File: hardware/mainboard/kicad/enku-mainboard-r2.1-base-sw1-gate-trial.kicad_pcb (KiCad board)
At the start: 4 copper layers, 59 x 101 mm, 132 parts, among them J1 1S LiPo + NTC, J2 Hirose DM3AT-SF-PEJM5, J3 FH34SRJ-24S-0.5SH(50), J5 GCT USB4105-GF-A-120, J6 4-pin pogo dock, J7 Tag-Connect TC2030-IDC-NL, Q1 IRLML6346TRPBF, Q2 AO3401A, SW1 HARD POWER, SW2 BOOT / RECOVERY, SW3 BTN_L1, SW4 BTN_L2, SW5 BTN_R1, SW6 BTN_R2, U1 ESP32-S3-WROOM-1-N16R8, U10 TLV3012BIDBVR, U2 TPS2121, U3 BQ25185DLHR, U4 TPS63802DLAR, U5 BMI270, U8 USBLC6-2SC6, U9 TMUX1101DBVR

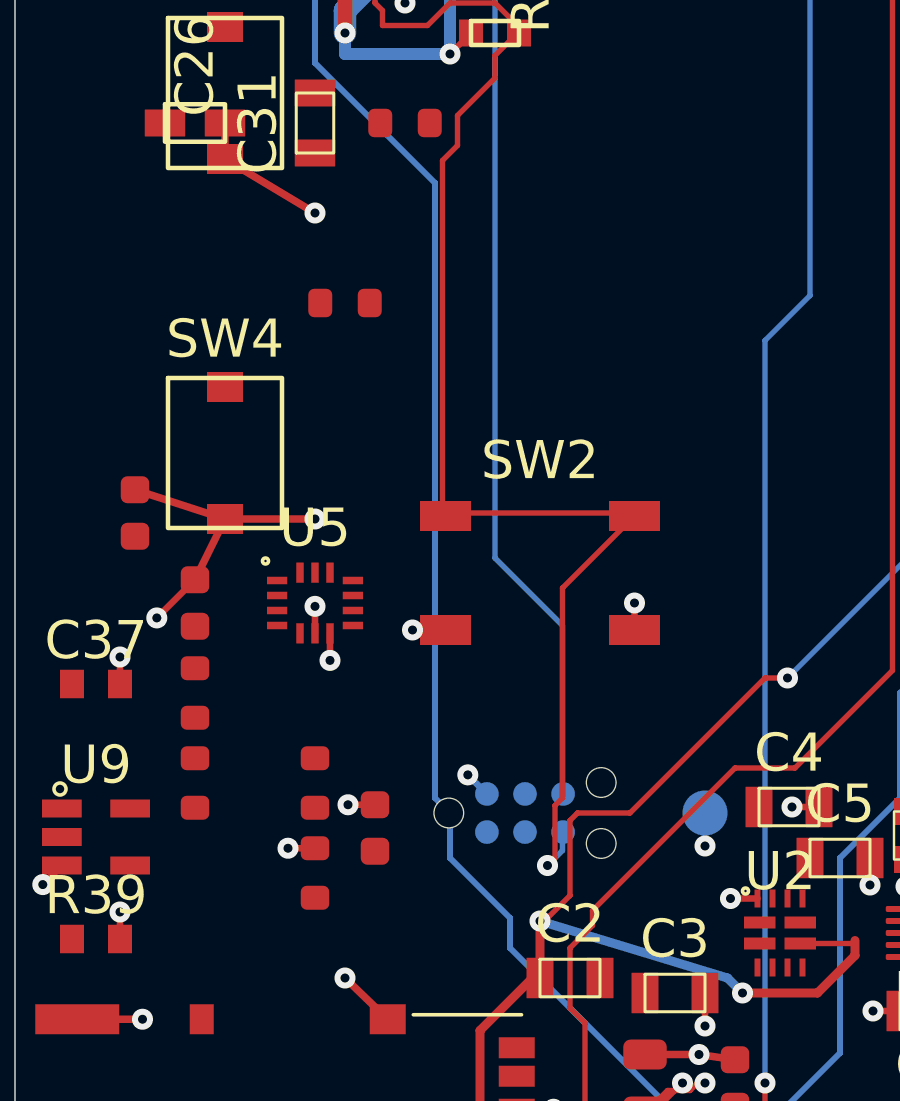
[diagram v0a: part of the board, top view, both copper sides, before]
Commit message: R44 DFM: reroute remote PMOS gate around J7 TagConnect NPTH guide holes; retain strict hole clearance checks
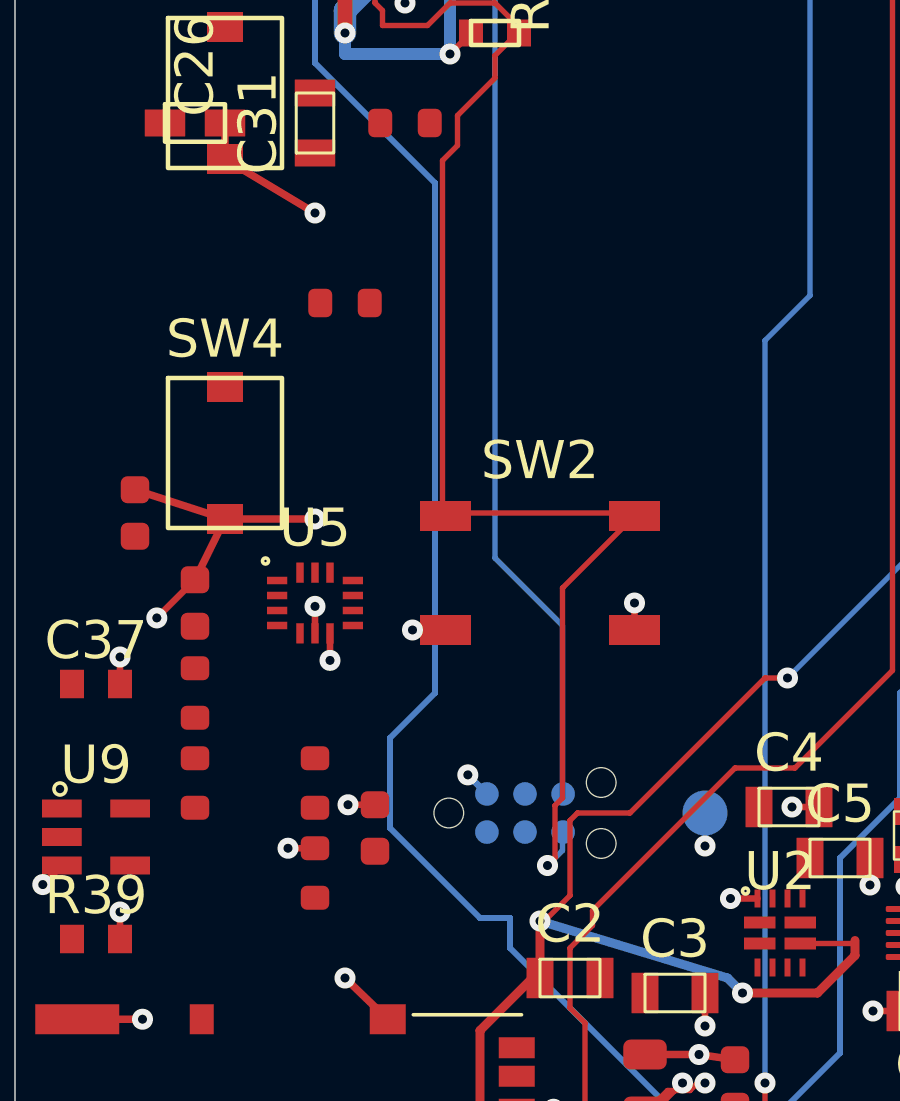
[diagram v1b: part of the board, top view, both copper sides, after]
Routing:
- net PWR_GATE: track 108.7 -> 110.5 mm
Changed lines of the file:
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@@
   (segment (start 28 59.5) (end 28 62) (width 0.20) (layer "B.Cu") (net 96))
   (segment (start 28 62) (end 32 66) (width 0.20) (layer "B.Cu") (net 96))
-  (segment (start 32 66) (end 32 86.5) (width 0.20) (layer "B.Cu") (net 96))
-  (segment (start 32 86.5) (end 32.5 87) (width 0.20) (layer "B.Cu") (net 96))
-  (segment (start 32.5 87) (end 32.5 88.5) (width 0.20) (layer "B.Cu") (net 96))
-  (segment (start 32.5 88.5) (end 34.5 90.5) (width 0.20) (layer "B.Cu") (net 96))
   (segment (start 34.5 90.5) (end 34.5 91.5) (width 0.20) (layer "B.Cu") (net 96))
   (segment (start 34.5 91.5) (end 39.5 96.5) (width 0.20) (layer "B.Cu") (net 96))
@@
   (via (at 53 79.5) (size 0.70) (drill 0.30) (layers "F.Cu" "B.Cu") (net 96))
   (via (at 47.5 36.5) (size 0.70) (drill 0.30) (layers "F.Cu" "B.Cu") (net 1))
+  (segment (start 32 66) (end 32 83) (width 0.20) (layer "B.Cu") (net 96))
+  (segment (start 32 83) (end 30.5 84.5) (width 0.20) (layer "B.Cu") (net 96))
+  (segment (start 30.5 84.5) (end 30.5 87.5) (width 0.20) (layer "B.Cu") (net 96))
+  (segment (start 30.5 87.5) (end 33.5 90.5) (width 0.20) (layer "B.Cu") (net 96))
+  (segment (start 33.5 90.5) (end 34.5 90.5) (width 0.20) (layer "B.Cu") (net 96))
 )
